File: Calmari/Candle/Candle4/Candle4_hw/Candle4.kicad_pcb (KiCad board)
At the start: 2 copper layers, 110 x 15 mm, 56 parts, among them Q1 LED_RGB, SW1 BUTTON, SW2 BUTTON, SW3 BUTTON

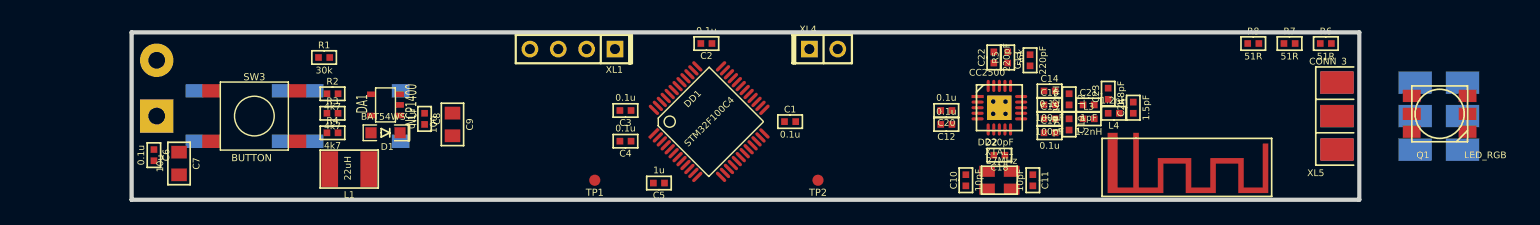
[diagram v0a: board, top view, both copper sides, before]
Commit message: Candle4 fsproj added
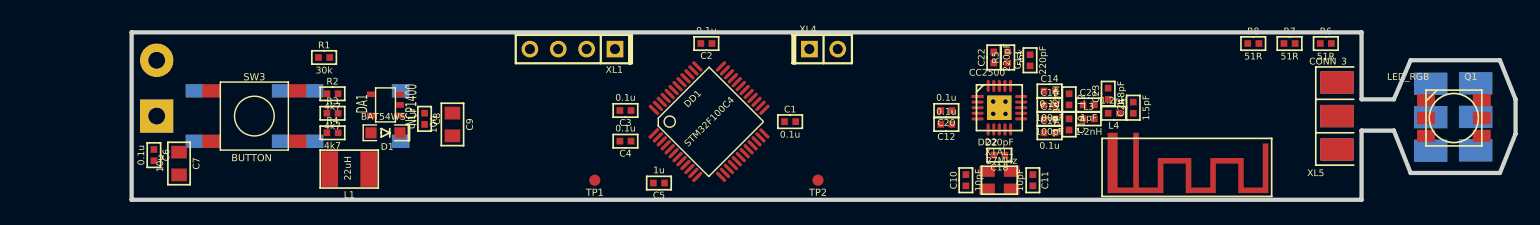
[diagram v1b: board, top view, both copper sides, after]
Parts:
- moved XL6 5.85 mm to (160.9, 69.6), turned to 180 degrees
- moved XL7 2.43 mm to (164.9, 69.6), turned to 180 degrees
- moved Q1 1.33 mm to (164.5, 69.7), turned to 0 degrees
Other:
- board size 110 x 15 mm -> 124 x 15 mm
- net class Default: clearance 0.254 -> 0.2; trace_width 0.254 -> 0.2; via_dia 0.889 -> 0.9; via_drill 0.635 -> 0.4
- net class Wide added: clearance 0.2, trace_width 0.5, via_dia 0.9, via_drill 0.4
- rule trace_clearance: 0.254 -> 0.2
- rule trace_min: 0.254 -> 0.2
- rule via_min_drill: 0.508 -> 0.4
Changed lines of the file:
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@@
     (links 144)
     (no_connects 144)
-    (area 0 0 0 0)
+    (area 45.809499 61.809499 156.190501 77.190501)
     (thickness 1.6)
-    (drawings 4)
+    (drawings 14)
     (tracks 0)
     (zones 0)
@@
   )
   (setup
-    (last_trace_width 0.254)
-    (trace_clearance 0.254)
+    (last_trace_width 0.2)
+    (trace_clearance 0.2)
     (zone_clearance 0.508)
     (zone_45_only no)
-    (trace_min 0.254)
+    (trace_min 0.2)
     (segment_width 0.15)
     (edge_width 0.381)
-    (via_size 0.889)
-    (via_drill 0.635)
+    (via_size 0.9)
+    (via_drill 0.4)
     (via_min_size 0.889)
-    (via_min_drill 0.508)
+    (via_min_drill 0.4)
     (uvia_size 0.508)
     (uvia_drill 0.127)
@@
     (pad_to_mask_clearance 0.1)
     (aux_axis_origin 0 0)
-    (visible_elements FFFFF9BF)
+    (visible_elements 7FFFFBFF)
     (pcbplotparams
       (layerselection 3178497)
@@
   (net 39 N-0000037)
   (net_class Default "This is the default net class."
-    (clearance 0.254)
-    (trace_width 0.254)
-    (via_dia 0.889)
-    (via_drill 0.635)
+    (clearance 0.2)
+    (trace_width 0.2)
+    (via_dia 0.9)
+    (via_drill 0.4)
     (uvia_dia 0.508)
     (uvia_drill 0.127)
     (add_net "")
-    (add_net +3.3V)
     (add_net /Ant1)
     (add_net /Ant2)
-    (add_net /BATT)
     (add_net /BTN_DOWN)
     (add_net /BTN_TX)
@@
     (add_net /LED_G)
     (add_net /LED_R)
-    (add_net /Lout)
     (add_net /SWCLK)
     (add_net /SWDIO)
     (add_net /WKUP)
-    (add_net GND)
     (add_net N-000001)
     (add_net N-0000011)
@@
     (add_net N-0000037)
   )
+  (net_class Wide ""
+    (clearance 0.2)
+    (trace_width 0.5)
+    (via_dia 0.9)
+    (via_drill 0.4)
+    (uvia_dia 0.508)
+    (uvia_drill 0.127)
+    (add_net +3.3V)
+    (add_net /BATT)
+    (add_net /Lout)
+    (add_net GND)
+  )
   (module TESTPOINT_1MM (layer F.Cu)
     (at 107.5 75.25)
@@
       (scale (xyz 1 1 1))
       (rotate (xyz 0 0 90))
-    )
-  )
-  (module LED_HH5050_RGB (layer F.Cu)
-    (at 163.2 69.3 180)
-    (fp_text reference Q1 (at 1.50114 -3.70078 180) (layer F.SilkS)
-      (effects (font (size 0.59944 0.59944) (thickness 0.14986)))
-    )
-    (fp_text value LED_RGB (at -4.09956 -3.70078 180) (layer F.SilkS)
-      (effects (font (size 0.59944 0.59944) (thickness 0.14986)))
-    )
-    (fp_line (start -2.5 -1.5) (end -1.5 -2.5) (layer F.SilkS) (width 0.15))
-    (fp_circle (center 0 0) (end 0 2.19964) (layer F.SilkS) (width 0.14986))
-    (fp_line (start 2.49936 -2.49936) (end 2.49936 2.49936) (layer F.SilkS) (width 0.14986))
-    (fp_line (start 2.49936 2.49936) (end -2.49936 2.49936) (layer F.SilkS) (width 0.14986))
-    (fp_line (start -2.49936 2.49936) (end -2.49936 -2.49936) (layer F.SilkS) (width 0.14986))
-    (fp_line (start -2.49936 -2.49936) (end 2.49936 -2.49936) (layer F.SilkS) (width 0.14986))
-    (pad GC smd rect (at 2.5 -1.6 180) (size 1.6 1.1)
-      (layers F.Cu F.Paste F.Mask)
-      (net 33 N-0000031)
-    )
-    (pad RC smd rect (at 2.5 0 180) (size 1.6 1.1)
-      (layers F.Cu F.Paste F.Mask)
-      (net 25 N-0000024)
-    )
-    (pad BC smd rect (at 2.5 1.6 180) (size 1.6 1.1)
-      (layers F.Cu F.Paste F.Mask)
-      (net 26 N-0000025)
-    )
-    (pad GA smd rect (at -2.5 -1.6 180) (size 1.6 1.1)
-      (layers F.Cu F.Paste F.Mask)
-      (net 27 N-0000026)
-    )
-    (pad RA smd rect (at -2.5 0 180) (size 1.6 1.1)
-      (layers F.Cu F.Paste F.Mask)
-      (net 28 N-0000027)
-    )
-    (pad BA smd rect (at -2.5 1.6 180) (size 1.6 1.1)
-      (layers F.Cu F.Paste F.Mask)
-      (net 24 N-0000023)
     )
   )
@@
   )
   (module CONN_SOLDER3 (layer B.Cu)
-    (at 166.75 69.5)
+    (at 160.9 69.6 180)
     (descr "Connector to solder PCBs together")
-    (fp_text reference XL6 (at -3.4 -5.1) (layer B.SilkS)
+    (fp_text reference XL6 (at -3.4 -5.1 180) (layer B.SilkS)
       (effects (font (size 0.6 0.6) (thickness 0.15)) (justify mirror))
     )
-    (fp_text value CONN_3 (at -2.3 4.9) (layer B.SilkS)
+    (fp_text value CONN_3 (at -2.3 4.9 180) (layer B.SilkS)
       (effects (font (size 0.6 0.6) (thickness 0.15)) (justify mirror))
     )
@@
     (fp_line (start -3.4 4.4) (end -3.4 -4.4) (layer B.SilkS) (width 0.15))
     (fp_line (start -3.4 -4.4) (end 0 -4.4) (layer B.SilkS) (width 0.15))
-    (pad 1 smd rect (at -1.5 3) (size 3 2)
+    (pad 1 smd rect (at -1.5 3 180) (size 3 2)
       (layers B.Cu B.Paste B.Mask)
       (net 28 N-0000027)
     )
-    (pad 2 smd rect (at -1.5 0) (size 3 2)
+    (pad 2 smd rect (at -1.5 0 180) (size 3 2)
       (layers B.Cu B.Paste B.Mask)
       (net 27 N-0000026)
     )
-    (pad 3 smd rect (at -1.5 -3) (size 3 2)
+    (pad 3 smd rect (at -1.5 -3 180) (size 3 2)
       (layers B.Cu B.Paste B.Mask)
       (net 24 N-0000023)
@@
   )
   (module CONN_SOLDER3 (layer B.Cu)
-    (at 162.5 69.5)
+    (at 164.925 69.575 180)
     (descr "Connector to solder PCBs together")
-    (fp_text reference XL7 (at -3.4 -5.1) (layer B.SilkS)
+    (fp_text reference XL7 (at -3.4 -5.1 180) (layer B.SilkS)
       (effects (font (size 0.6 0.6) (thickness 0.15)) (justify mirror))
     )
-    (fp_text value CONN_3 (at -2.3 4.9) (layer B.SilkS)
+    (fp_text value CONN_3 (at -2.3 4.9 180) (layer B.SilkS)
       (effects (font (size 0.6 0.6) (thickness 0.15)) (justify mirror))
     )
@@
     (fp_line (start -3.4 4.4) (end -3.4 -4.4) (layer B.SilkS) (width 0.15))
     (fp_line (start -3.4 -4.4) (end 0 -4.4) (layer B.SilkS) (width 0.15))
-    (pad 1 smd rect (at -1.5 3) (size 3 2)
+    (pad 1 smd rect (at -1.5 3 180) (size 3 2)
       (layers B.Cu B.Paste B.Mask)
       (net 25 N-0000024)
     )
-    (pad 2 smd rect (at -1.5 0) (size 3 2)
+    (pad 2 smd rect (at -1.5 0 180) (size 3 2)
       (layers B.Cu B.Paste B.Mask)
       (net 33 N-0000031)
     )
-    (pad 3 smd rect (at -1.5 -3) (size 3 2)
+    (pad 3 smd rect (at -1.5 -3 180) (size 3 2)
       (layers B.Cu B.Paste B.Mask)
       (net 26 N-0000025)
@@
     )
   )
-  (gr_line (start 46 62) (end 156 62) (angle 90) (layer Edge.Cuts) (width 0.381))
+  (module LED_HH5050_RGB (layer F.Cu)
+    (at 164.475 69.675)
+    (fp_text reference Q1 (at 1.50114 -3.70078) (layer F.SilkS)
+      (effects (font (size 0.59944 0.59944) (thickness 0.14986)))
+    )
+    (fp_text value LED_RGB (at -4.09956 -3.70078) (layer F.SilkS)
+      (effects (font (size 0.59944 0.59944) (thickness 0.14986)))
+    )
+    (fp_line (start -2.5 -1.5) (end -1.5 -2.5) (layer F.SilkS) (width 0.15))
+    (fp_circle (center 0 0) (end 0 2.19964) (layer F.SilkS) (width 0.14986))
+    (fp_line (start 2.49936 -2.49936) (end 2.49936 2.49936) (layer F.SilkS) (width 0.14986))
+    (fp_line (start 2.49936 2.49936) (end -2.49936 2.49936) (layer F.SilkS) (width 0.14986))
+    (fp_line (start -2.49936 2.49936) (end -2.49936 -2.49936) (layer F.SilkS) (width 0.14986))
+    (fp_line (start -2.49936 -2.49936) (end 2.49936 -2.49936) (layer F.SilkS) (width 0.14986))
+    (pad BC smd rect (at 2.5 -1.6) (size 1.6 1.1)
+      (layers F.Cu F.Paste F.Mask)
+      (net 26 N-0000025)
+    )
+    (pad RC smd rect (at 2.5 0) (size 1.6 1.1)
+      (layers F.Cu F.Paste F.Mask)
+      (net 25 N-0000024)
+    )
+    (pad GC smd rect (at 2.5 1.6) (size 1.6 1.1)
+      (layers F.Cu F.Paste F.Mask)
+      (net 33 N-0000031)
+    )
+    (pad BA smd rect (at -2.5 -1.6) (size 1.6 1.1)
+      (layers F.Cu F.Paste F.Mask)
+      (net 24 N-0000023)
+    )
+    (pad RA smd rect (at -2.5 0) (size 1.6 1.1)
+      (layers F.Cu F.Paste F.Mask)
+      (net 28 N-0000027)
+    )
+    (pad GA smd rect (at -2.5 1.6) (size 1.6 1.1)
+      (layers F.Cu F.Paste F.Mask)
+      (net 27 N-0000026)
+    )
+  )
+  (gr_line (start 156.2 62) (end 156.2 68) (angle 90) (layer Edge.Cuts) (width 0.381))
+  (gr_line (start 46 62) (end 156.2 62) (angle 90) (layer Edge.Cuts) (width 0.381))
   (gr_line (start 46 77) (end 46 62) (angle 90) (layer Edge.Cuts) (width 0.381))
-  (gr_line (start 156 77) (end 46 77) (angle 90) (layer Edge.Cuts) (width 0.381))
-  (gr_line (start 156 62) (end 156 77) (angle 90) (layer Edge.Cuts) (width 0.381))
+  (gr_line (start 156.2 77) (end 46 77) (angle 90) (layer Edge.Cuts) (width 0.381))
+  (gr_line (start 156.2 70.8) (end 156.2 77) (angle 90) (layer Edge.Cuts) (width 0.381))
+  (gr_line (start 159.1 70.8) (end 156.2 70.8) (angle 90) (layer Edge.Cuts) (width 0.381))
+  (gr_line (start 160.6 74.6) (end 159.1 70.8) (angle 90) (layer Edge.Cuts) (width 0.381))
+  (gr_line (start 168.6 74.6) (end 160.6 74.6) (angle 90) (layer Edge.Cuts) (width 0.381))
+  (gr_line (start 170 71.1) (end 168.6 74.6) (angle 90) (layer Edge.Cuts) (width 0.381))
+  (gr_line (start 170 68) (end 170 71.1) (angle 90) (layer Edge.Cuts) (width 0.381))
+  (gr_line (start 168.6 64.5) (end 170 68) (angle 90) (layer Edge.Cuts) (width 0.381))
+  (gr_line (start 160.6 64.5) (end 168.6 64.5) (angle 90) (layer Edge.Cuts) (width 0.381))
+  (gr_line (start 159.1 68) (end 160.6 64.5) (angle 90) (layer Edge.Cuts) (width 0.381))
+  (gr_line (start 156.2 68) (end 159.1 68) (angle 90) (layer Edge.Cuts) (width 0.381))
 )

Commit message: 
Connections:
- ANT1 pad 1: N-0000035 (its old number) -> GND
- C24 pad 1: N-0000035 (its old number) -> GND
- L4 pad 1: N-0000035 (its old number) -> GND

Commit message: gerber added
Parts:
- moved SW3 11.1 mm to (45.9, 70.6)
- moved R2 10.6 mm to (71.1, 75.4)
- moved XL3 9.68 mm to (38.6, 65.6)
- moved XL2 9.64 mm to (38.6, 70.3)
- moved C7 8.21 mm to (57.8, 70.6), turned to 90 degrees
- moved C6 7.62 mm to (55.2, 70.6), turned to 90 degrees
- moved R8 5.12 mm to (141.5, 64.1)
- moved C2 5.11 mm to (102.2, 65.1), turned to 0 degrees
- moved TP1 4.49 mm to (91.8, 73.9)
- moved R7 4.37 mm to (145.5, 64.1)
- moved R6 3.71 mm to (149.5, 64.2)
- moved R1 2.85 mm to (60.9, 65.8), turned to 90 degrees
- moved L2 2.53 mm to (130.0, 70.5), turned to 90 degrees
- moved C19 1.99 mm to (130.0, 68.3), turned to 90 degrees
- moved C8 1.55 mm to (73.8, 69.9)
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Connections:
- ANT1 pad 1: GND -> N-0000035
- C24 pad 1: GND -> N-0000035
- L4 pad 1: GND -> N-0000035
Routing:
- net GND: track 0.00 -> 308.6 mm, vias 0 -> 56
- net +3.3V: track 0.00 -> 160.3 mm, vias 0 -> 5
- net /WKUP: track 0.00 -> 71.9 mm, vias 0 -> 3
- net /BTN_TX: track 0.00 -> 60.9 mm
- net /LED_R: track 0.00 -> 50.9 mm, vias 0 -> 2
- net /LED_G: track 0.00 -> 48.4 mm, vias 0 -> 2
- net /LED_B: track 0.00 -> 46.6 mm, vias 0 -> 2
- net /BTN_DOWN: track 0.00 -> 46.1 mm, vias 0 -> 2
- net /BTN_UP: track 0.00 -> 38.6 mm, vias 0 -> 2
- net /BATT: track 0.00 -> 26.6 mm
- net /CC_CS: track 0.00 -> 25.8 mm
- net /CC_MOSI: track 0.00 -> 25.2 mm, vias 0 -> 2
- net /CC_SCK: track 0.00 -> 25.1 mm, vias 0 -> 2
- net /CC_GDO0: track 0.00 -> 24.9 mm
- net /CC_MISO: track 0.00 -> 24.2 mm, vias 0 -> 2
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- added copper zone on B.Cu, net GND
- added copper zone on F.Cu, net GND
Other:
- board size 124 x 15 mm -> 133.6 x 13.8 mm
- board text added: "+"
